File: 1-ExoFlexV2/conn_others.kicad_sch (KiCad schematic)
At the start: 10 parts, among them J61 1751112, J62 POS_LC1, J63 POS_LC1

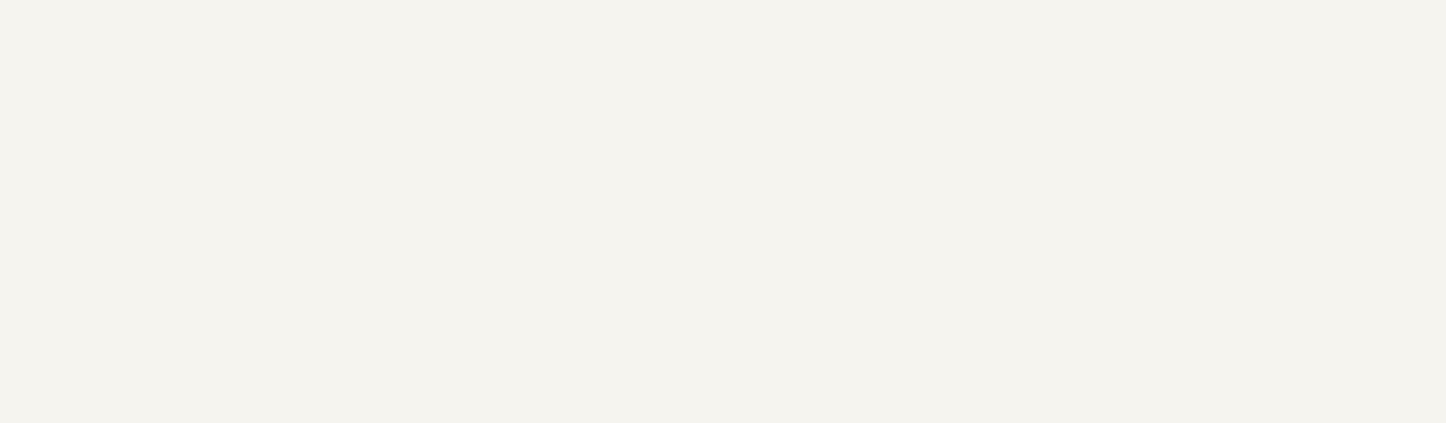
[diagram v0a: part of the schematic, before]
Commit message: Test points et notes
- Ajout de tous les tests point nécessaires
-  Ajoute des sections de notes dans chaque page
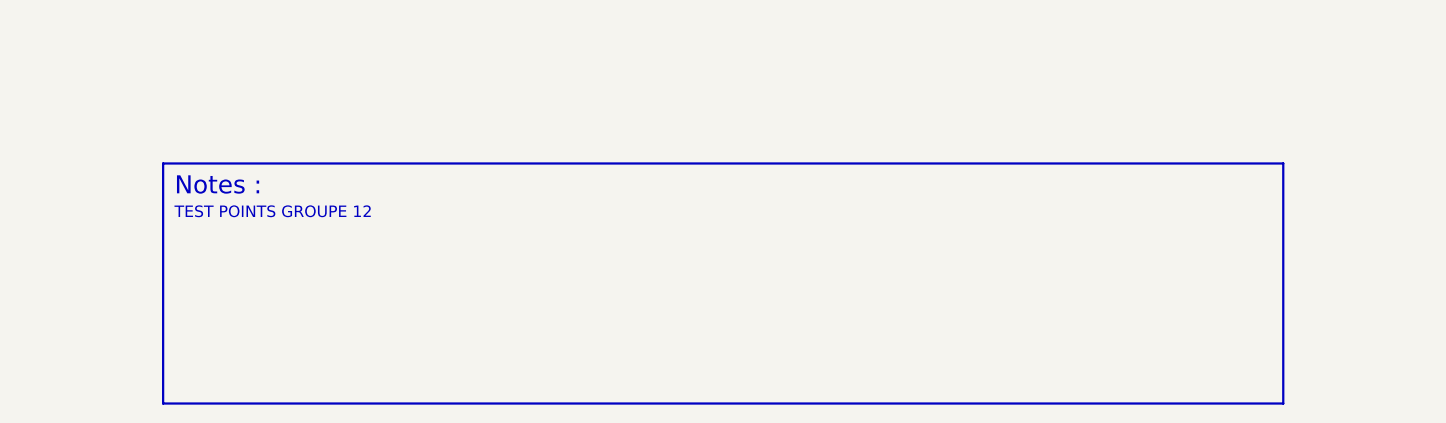
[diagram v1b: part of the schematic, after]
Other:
- note added: "Notes :"
- note added: "TEST POINTS GROUPE 12"
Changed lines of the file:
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@@
     (stroke (width 0) (type default) (color 0 0 0 0))
+  )
+  (polyline (pts (xy 173.99 194.31) (xy 49.53 194.31))
+    (stroke (width 0.25) (type solid) (color 0 0 0 0))
+  )
+  (polyline (pts (xy 173.99 167.64) (xy 173.99 194.31))
+    (stroke (width 0.25) (type solid) (color 0 0 0 0))
+  )
+  (polyline (pts (xy 49.53 167.64) (xy 173.99 167.64))
+    (stroke (width 0.25) (type solid) (color 0 0 0 0))
   )
   (wire (pts (xy 134.62 88.9) (xy 154.94 88.9))
@@
   (wire (pts (xy 234.95 86.36) (xy 246.38 86.36))
     (stroke (width 0) (type default) (color 0 0 0 0))
+  )
+  (polyline (pts (xy 49.53 167.64) (xy 49.53 194.31))
+    (stroke (width 0.25) (type solid) (color 0 0 0 0))
   )
   (wire (pts (xy 48.26 90.17) (xy 43.18 90.17))
@@
     (stroke (width 0) (type default) (color 0 0 0 0))
   )
+  (text "TEST POINTS GROUPE 12" (at 50.8 173.99 0)
+    (effects (font (size 1.27 1.27)) (justify left bottom))
+  )
+  (text "Notes :" (at 50.8 171.45 0)
+    (effects (font (size 2 2)) (justify left bottom))
+  )
   (text "Bus Adapter : 5V @ 75mA\n2xTempSensor : N/A (uA)\n\nTotal current : 5V @ 75mA"

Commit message: Schématisation terminée
- Schéma terminé
- Passage vers le PCB
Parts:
- D100: renamed from D101; value TPD1E -> TVS; DESCRIPTION (none) -> TVS DIODE 5.5VWM 14VC 2X1SON; MANUFACTURER (none) -> Texas Instruments; PACKAGE (none) -> 0402 (1006 Metric); PART NUMBER (none) -> TPD1E05U06DPYR; TYPE (none) -> SMD
- D101: renamed from D102; value TPD1E -> TVS; DESCRIPTION (none) -> TVS DIODE 5.5VWM 14VC 2X1SON; MANUFACTURER (none) -> Texas Instruments; PACKAGE (none) -> 0402 (1006 Metric); PART NUMBER (none) -> TPD1E05U06DPYR; TYPE (none) -> SMD
- D102: renamed from D103; value TPD1E -> TVS; DESCRIPTION (none) -> TVS DIODE 5.5VWM 14VC 2X1SON; MANUFACTURER (none) -> Texas Instruments; PACKAGE (none) -> 0402 (1006 Metric); PART NUMBER (none) -> TPD1E05U06DPYR; TYPE (none) -> SMD
- D103: renamed from D104; value TPD1E -> TVS; DESCRIPTION (none) -> TVS DIODE 5.5VWM 14VC 2X1SON; MANUFACTURER (none) -> Texas Instruments; PACKAGE (none) -> 0402 (1006 Metric); PART NUMBER (none) -> TPD1E05U06DPYR; TYPE (none) -> SMD
- D104: renamed from D105; value TPD1E -> TVS; DESCRIPTION (none) -> TVS DIODE 5.5VWM 14VC 2X1SON; MANUFACTURER (none) -> Texas Instruments; PACKAGE (none) -> 0402 (1006 Metric); PART NUMBER (none) -> TPD1E05U06DPYR; TYPE (none) -> SMD
- D105: renamed from D106; value TPD1E -> TVS; DESCRIPTION (none) -> TVS DIODE 5.5VWM 14VC 2X1SON; MANUFACTURER (none) -> Texas Instruments; PACKAGE (none) -> 0402 (1006 Metric); PART NUMBER (none) -> TPD1E05U06DPYR; TYPE (none) -> SMD
- D106: renamed from D107; value TPD1E -> TVS; DESCRIPTION (none) -> TVS DIODE 5.5VWM 14VC 2X1SON; MANUFACTURER (none) -> Texas Instruments; PACKAGE (none) -> 0402 (1006 Metric); PART NUMBER (none) -> TPD1E05U06DPYR; TYPE (none) -> SMD
- J56: renamed from J61; value 1751112 -> 4; DESCRIPTION (none) -> 4 Position Wire to Board Terminal Block 55° (125°) Angle wi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; PACKAGE (none) -> 4 POS 0.100" (2.54mm); PART NUMBER (none) -> 1751112; TYPE (none) -> Through Hole
- J57: renamed from J62; value POS_LC1 -> 3; DESCRIPTION (none) -> 3 Position Wire to Board Terminal Block 55° (125°) Angle wi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; PACKAGE (none) -> 3 POS 0.100" (2.54mm); PART NUMBER (none) -> 1751109; TYPE (none) -> Through Hole
- J58: renamed from J63; value POS_LC1 -> 3; DESCRIPTION (none) -> 3 Position Wire to Board Terminal Block 55° (125°) Angle wi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; PACKAGE (none) -> 3 POS 0.100" (2.54mm); PART NUMBER (none) -> 1751109; TYPE (none) -> Through Hole
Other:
- note added: "Bus Adapter : 5V @ 75mA 2xTempSensor : N/A (uA) Total current : 5V @ 80mA"
- note added: "CAN Bus"
- note added: "Temp 1"
- note added: "Temp 2"
- note removed: "Bus Adapter : 5V @ 75mA 2xTempSensor : N/A (uA) Total current : 5V @ 75mA"

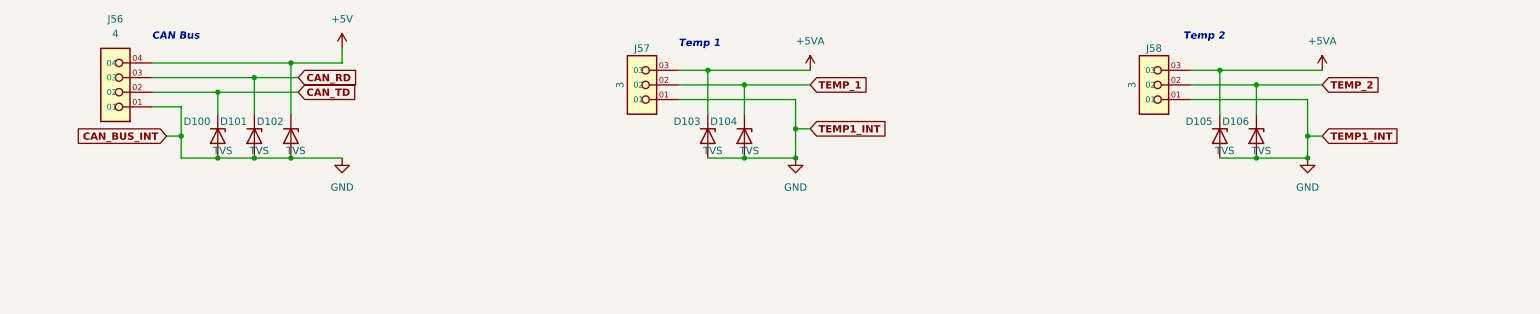
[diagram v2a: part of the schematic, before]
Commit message: Bug NetList
- Ajout de net-tie pour les GND et et les +5V
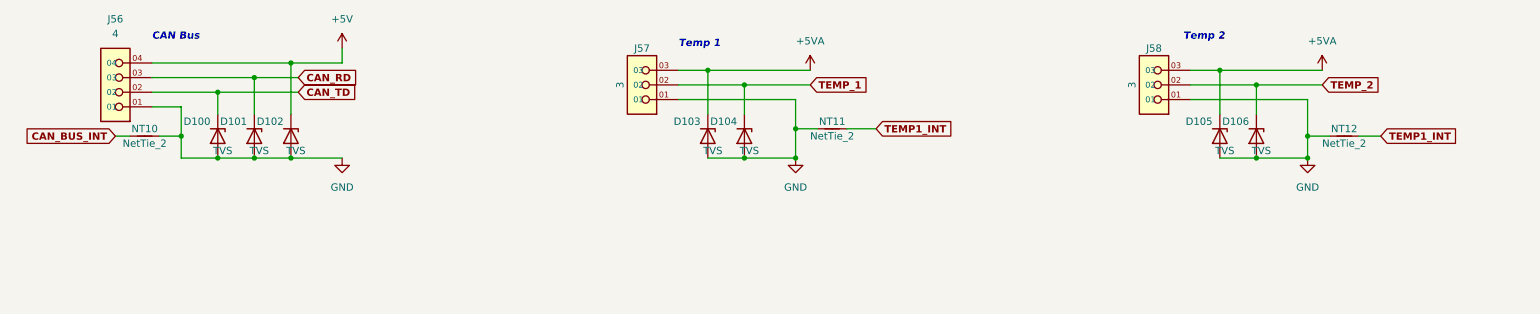
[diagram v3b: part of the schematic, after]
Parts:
- added NT10, NT11, NT12: NetTie_2, NetTie:NetTie-2_SMD_Pad0.5mm, symbol Device:NetTie_2
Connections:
- net GND: now also NT10.2, NT11.1, NT12.1
- new net CAN_BUS_INT: NT10.1
- new net TEMP1_INT: NT11.2, NT12.2
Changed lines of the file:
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@@
   (junction (at 48.26 95.25) (diameter 0) (color 0 0 0 0)
   )
+  (junction (at 243.84 99.06) (diameter 0) (color 0 0 0 0)
+  )
   (junction (at 154.94 93.98) (diameter 0) (color 0 0 0 0)
   )
@@
   (junction (at 243.84 95.25) (diameter 0) (color 0 0 0 0)
   )
-  (junction (at 243.84 99.06) (diameter 0) (color 0 0 0 0)
-  )
   (junction (at 234.95 99.06) (diameter 0) (color 0 0 0 0)
   )
   (junction (at 139.7 83.82) (diameter 0) (color 0 0 0 0)
   )
+  (junction (at 154.94 99.06) (diameter 0) (color 0 0 0 0)
+  )
   (junction (at 234.95 86.36) (diameter 0) (color 0 0 0 0)
   )
@@
   )
   (junction (at 54.61 99.06) (diameter 0) (color 0 0 0 0)
-  )
-  (junction (at 154.94 99.06) (diameter 0) (color 0 0 0 0)
   )
   (junction (at 67.31 82.55) (diameter 0) (color 0 0 0 0)
@@
     (stroke (width 0) (type default) (color 0 0 0 0))
   )
+  (wire (pts (xy 163.83 93.98) (xy 168.91 93.98))
+    (stroke (width 0) (type default) (color 0 0 0 0))
+  )
   (wire (pts (xy 48.26 90.17) (xy 48.26 95.25))
     (stroke (width 0) (type default) (color 0 0 0 0))
   )
   (wire (pts (xy 234.95 86.36) (xy 246.38 86.36))
+    (stroke (width 0) (type default) (color 0 0 0 0))
+  )
+  (wire (pts (xy 252.73 95.25) (xy 256.54 95.25))
     (stroke (width 0) (type default) (color 0 0 0 0))
   )
@@
     (stroke (width 0) (type default) (color 0 0 0 0))
   )
-  (wire (pts (xy 154.94 93.98) (xy 157.48 93.98))
+  (wire (pts (xy 154.94 93.98) (xy 158.75 93.98))
     (stroke (width 0) (type default) (color 0 0 0 0))
   )
@@
     (stroke (width 0) (type default) (color 0 0 0 0))
   )
-  (wire (pts (xy 45.72 95.25) (xy 48.26 95.25))
+  (wire (pts (xy 36.83 95.25) (xy 39.37 95.25))
     (stroke (width 0) (type default) (color 0 0 0 0))
   )
@@
     (stroke (width 0) (type default) (color 0 0 0 0))
   )
+  (wire (pts (xy 44.45 95.25) (xy 48.26 95.25))
+    (stroke (width 0) (type default) (color 0 0 0 0))
+  )
   (wire (pts (xy 48.26 99.06) (xy 54.61 99.06))
     (stroke (width 0) (type default) (color 0 0 0 0))
@@
     (stroke (width 0) (type default) (color 0 0 0 0))
   )
-  (wire (pts (xy 243.84 95.25) (xy 246.38 95.25))
+  (wire (pts (xy 243.84 95.25) (xy 247.65 95.25))
     (stroke (width 0) (type default) (color 0 0 0 0))
   )
@@
     )
   )
-  (global_label "CAN_BUS_INT" (shape input) (at 45.72 95.25 180) (fields_autoplaced)
+  (global_label "CAN_BUS_INT" (shape input) (at 36.83 95.25 180) (fields_autoplaced)
     (effects (font (size 1.27 1.27) bold) (justify right))
-    (property "Intersheet References" "${INTERSHEET_REFS}" (id 0) (at 30.5889 95.123 0)
+    (property "Intersheet References" "${INTERSHEET_REFS}" (id 0) (at 21.6989 95.123 0)
       (effects (font (size 1.27 1.27) bold) (justify right) hide)
     )
@@
     )
   )
-  (global_label "TEMP1_INT" (shape input) (at 157.48 93.98 0) (fields_autoplaced)
+  (global_label "TEMP1_INT" (shape input) (at 168.91 93.98 0) (fields_autoplaced)
     (effects (font (size 1.27 1.27) bold) (justify left))
-    (property "Intersheet References" "${INTERSHEET_REFS}" (id 0) (at 170.1921 93.853 0)
+    (property "Intersheet References" "${INTERSHEET_REFS}" (id 0) (at 181.6221 93.853 0)
       (effects (font (size 1.27 1.27) bold) (justify left) hide)
     )
@@
     )
   )
-  (global_label "TEMP1_INT" (shape input) (at 246.38 95.25 0) (fields_autoplaced)
+  (global_label "TEMP1_INT" (shape input) (at 256.54 95.25 0) (fields_autoplaced)
     (effects (font (size 1.27 1.27) bold) (justify left))
-    (property "Intersheet References" "${INTERSHEET_REFS}" (id 0) (at 259.0921 95.123 0)
+    (property "Intersheet References" "${INTERSHEET_REFS}" (id 0) (at 269.2521 95.123 0)
       (effects (font (size 1.27 1.27) bold) (justify left) hide)
     )
@@
   (symbol (lib_id "power:+5VA") (at 246.38 83.82 0) (unit 1)
     (in_bom yes) (on_board yes) (fields_autoplaced)
-    (property "Reference" "#PWR0135" (id 0) (at 246.38 87.63 0)
+    (property "Reference" "#PWR0136" (id 0) (at 246.38 87.63 0)
       (effects (font (size 1.27 1.27)) hide)
     )
@@
     (pin "04")
   )
+  (symbol (lib_id "Device:NetTie_2") (at 250.19 95.25 0) (unit 1)
+    (in_bom no) (on_board yes)
+    (property "Reference" "NT12" (id 0) (at 250.19 93.98 0))
+    (property "Value" "NetTie_2" (id 1) (at 250.19 96.52 0))
+    (property "Footprint" "NetTie:NetTie-2_SMD_Pad0.5mm" (id 2) (at 250.19 95.25 0)
+      (effects (font (size 1.27 1.27)) hide)
+    )
+    (property "Datasheet" "~" (id 3) (at 250.19 95.25 0)
+      (effects (font (size 1.27 1.27)) hide)
+    )
+    (pin "1")
+    (pin "2")
+  )
   (symbol (lib_id "Device:D_Zener") (at 54.61 95.25 270) (unit 1)
     (in_bom yes) (on_board yes)
@@
     (pin "2")
   )
-  (symbol (lib_id "power:GND") (at 243.84 99.06 0) (unit 1)
-    (in_bom yes) (on_board yes) (fields_autoplaced)
-    (property "Reference" "#PWR0134" (id 0) (at 243.84 105.41 0)
-      (effects (font (size 1.27 1.27)) hide)
-    )
-    (property "Value" "GND" (id 1) (at 243.84 104.14 0))
-    (property "Footprint" "" (id 2) (at 243.84 99.06 0)
-      (effects (font (size 1.27 1.27)) hide)
-    )
-    (property "Datasheet" "" (id 3) (at 243.84 99.06 0)
-      (effects (font (size 1.27 1.27)) hide)
-    )
-    (pin "1")
+  (symbol (lib_id "Device:NetTie_2") (at 41.91 95.25 0) (unit 1)
+    (in_bom no) (on_board yes)
+    (property "Reference" "NT10" (id 0) (at 41.91 93.98 0))
+    (property "Value" "NetTie_2" (id 1) (at 41.91 96.52 0))
+    (property "Footprint" "NetTie:NetTie-2_SMD_Pad0.5mm" (id 2) (at 41.91 95.25 0)
+      (effects (font (size 1.27 1.27)) hide)
+    )
+    (property "Datasheet" "~" (id 3) (at 41.91 95.25 0)
+      (effects (font (size 1.27 1.27)) hide)
+    )
+    (pin "1")
+    (pin "2")
   )
   (symbol (lib_id "SymLib:1751109") (at 124.46 86.36 180) (unit 1)
@@
     (pin "03")
   )
+  (symbol (lib_id "power:GND") (at 76.2 99.06 0) (unit 1)
+    (in_bom yes) (on_board yes) (fields_autoplaced)
+    (property "Reference" "#PWR0124" (id 0) (at 76.2 105.41 0)
+      (effects (font (size 1.27 1.27)) hide)
+    )
+    (property "Value" "GND" (id 1) (at 76.2 104.14 0))
+    (property "Footprint" "" (id 2) (at 76.2 99.06 0)
+      (effects (font (size 1.27 1.27)) hide)
+    )
+    (property "Datasheet" "" (id 3) (at 76.2 99.06 0)
+      (effects (font (size 1.27 1.27)) hide)
+    )
+    (pin "1")
+  )
   (symbol (lib_id "Device:D_Zener") (at 67.31 95.25 270) (unit 1)
     (in_bom yes) (on_board yes)
@@
     )
     (property "TYPE" "SMD" (id 8) (at 67.31 95.25 0)
+      (effects (font (size 1.27 1.27)) hide)
+    )
+    (pin "1")
+    (pin "2")
+  )
+  (symbol (lib_id "Device:NetTie_2") (at 161.29 93.98 0) (unit 1)
+    (in_bom no) (on_board yes)
+    (property "Reference" "NT11" (id 0) (at 161.29 92.71 0))
+    (property "Value" "NetTie_2" (id 1) (at 161.29 95.25 0))
+    (property "Footprint" "NetTie:NetTie-2_SMD_Pad0.5mm" (id 2) (at 161.29 93.98 0)
+      (effects (font (size 1.27 1.27)) hide)
+    )
+    (property "Datasheet" "~" (id 3) (at 161.29 93.98 0)
       (effects (font (size 1.27 1.27)) hide)
     )
@@
   (symbol (lib_id "power:+5VA") (at 157.48 83.82 0) (unit 1)
     (in_bom yes) (on_board yes) (fields_autoplaced)
-    (property "Reference" "#PWR0133" (id 0) (at 157.48 87.63 0)
+    (property "Reference" "#PWR0134" (id 0) (at 157.48 87.63 0)
       (effects (font (size 1.27 1.27)) hide)
     )
@@
   (symbol (lib_id "power:+5V") (at 76.2 80.01 0) (unit 1)
     (in_bom yes) (on_board yes) (fields_autoplaced)
-    (property "Reference" "#PWR0130" (id 0) (at 76.2 83.82 0)
+    (property "Reference" "#PWR0131" (id 0) (at 76.2 83.82 0)
       (effects (font (size 1.27 1.27)) hide)
     )
@@
     (pin "1")
   )
-  (symbol (lib_id "power:GND") (at 76.2 99.06 0) (unit 1)
+  (symbol (lib_id "power:GND") (at 243.84 99.06 0) (unit 1)
     (in_bom yes) (on_board yes) (fields_autoplaced)
-    (property "Reference" "#PWR0131" (id 0) (at 76.2 105.41 0)
-      (effects (font (size 1.27 1.27)) hide)
-    )
-    (property "Value" "GND" (id 1) (at 76.2 104.14 0))
-    (property "Footprint" "" (id 2) (at 76.2 99.06 0)
-      (effects (font (size 1.27 1.27)) hide)
-    )
-    (property "Datasheet" "" (id 3) (at 76.2 99.06 0)
-      (effects (font (size 1.27 1.27)) hide)
-    )
+    (property "Reference" "#PWR0133" (id 0) (at 243.84 105.41 0)
+      (effects (font (size 1.27 1.27)) hide)
+    )
+    (property "Value" "GND" (id 1) (at 243.84 104.14 0))
+    (property "Footprint" "" (id 2) (at 243.84 99.06 0)
+      (effects (font (size 1.27 1.27)) hide)
+    )
+    (property "Datasheet" "" (id 3) (at 243.84 99.06 0)
+      (effects (font (size 1.27 1.27)) hide)
+    )
